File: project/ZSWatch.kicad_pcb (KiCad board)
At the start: 4 copper layers, 41 x 38 mm, 76 parts, among them IC1 nPM1300-QEXX, IC10 NTS0104GU12, IC11 FAN5622SX, IC2 APDS-9306-065, IC3 BMI270, IC4 BMP581, IC5 BME688, IC6 LIS2MDLTR, IC7 ESDALC6V1W5, IC8 AT25SL128A, IC9 DRV2603RUNT, M1 NORA-B106, X1 BATTERY, X10 GC9A01A_CST816S, X2 DOCK, X3 GPIO0, X4 GPIO1, X5 GPIO2, X6 GPIO3, X7 GND, X8 M+, X9 M-

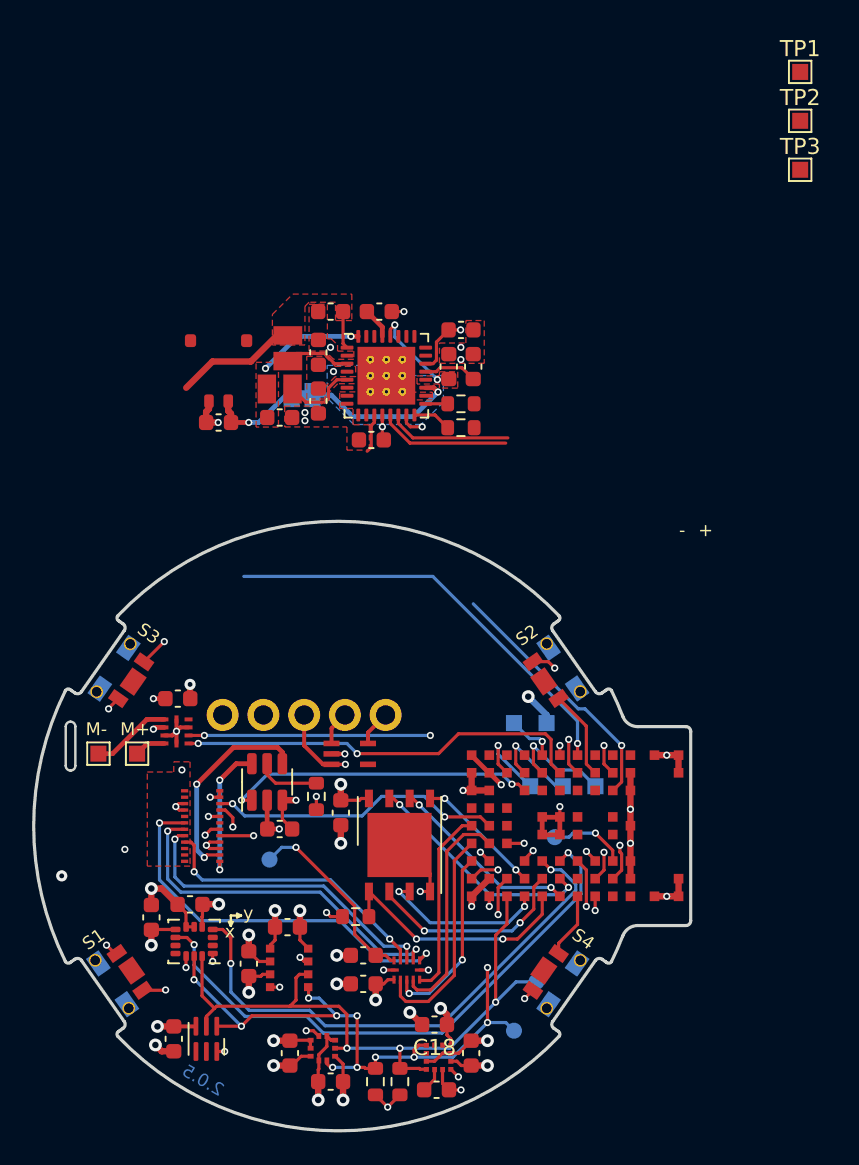
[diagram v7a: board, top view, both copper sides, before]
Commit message: - Add QR code library with link to the project - Change ISET resistor to 12k - Replace light sensor footprint with a version from our KiCad library - Rename the inner copper layers - Add KiBot file for production file generation - Import nPM1300 from test project - Remove pull down resistor from vibration driver IC enable - Split schematics into hierarical schematics - Add PCB variant for reduced sensor board - Add I2S microphone - Update all symbols and footprints
Signed-off-by: Daniel Kampert <DanielKampert@kampis-elektroecke.de>
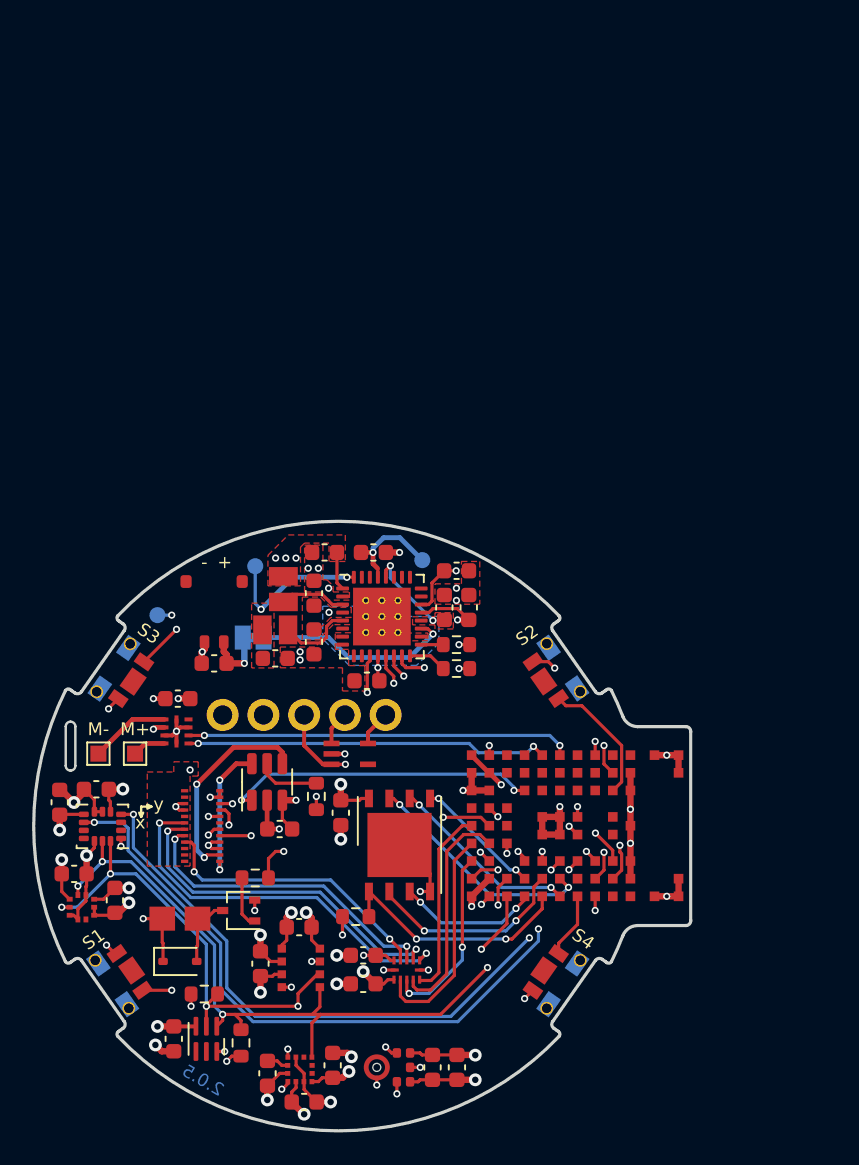
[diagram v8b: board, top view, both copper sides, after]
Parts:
- removed TP4: RESET, TestPoint:TestPoint_Pad_D1.0mm
- removed TP5: SCL, TestPoint:TestPoint_Pad_D1.0mm
- removed TP6: SDA, TestPoint:TestPoint_Pad_D1.0mm
- removed TP7: 3V3, TestPoint:TestPoint_Pad_D1.0mm
- removed the X3 at (171.3, 110.2)
- removed the X4 at (173.4, 110.2)
- removed the X5 at (175.4, 110.2)
- removed X6: GPIO3, TestPoint:TestPoint_Pad_1.0x1.0mm
- removed X7: GND, TestPoint:TestPoint_Pad_1.0x1.0mm
- added BZ1: Buzzer, CUI Devices:CMT-322-65-SMT-TR, F.Cu at (149.5, 118.5)
- added C22: 1u, Capacitor_SMD:C_0603_1608Metric, F.Cu at (165.2, 127.8)
- added C23: 200p, Capacitor_SMD:C_0603_1608Metric, F.Cu at (166.8, 127.8)
- added D1: BAS316, Diode_SMD:D_SOD-323, F.Cu at (149.5, 121.2)
- added MK1: SPH0645LM4H-B, Knowles:SPH0645LM4H-6_3.5x2.65mm, F.Cu at (162.5, 127.8)
- added Q1: BC817W, Package_TO_SOT_SMD:SOT-323_SC-70, F.Cu at (153.1, 118.0)
- added R6: 180R, Resistor_SMD:R_0603_1608Metric, F.Cu at (154.2, 116.0)
- TP1, TP2, TP3: footprint TestPoint:TestPoint_Pad_1.0x1.0mm -> TestPoint:TestPoint_Pad_D1.0mm; moved to B.Cu
- moved TP2 50.5 mm to (148.1, 99.6), turned to -90 degrees
- moved TP3 42.0 mm to (154.2, 96.5), turned to 180 degrees
- moved TP1 38.5 mm to (164.6, 96.1), turned to 180 degrees
- moved G*** 22.6 mm to (177.0, 112.6), turned to 90 degrees
- moved C15 20.6 mm to (142.9, 115.7), turned to 180 degrees
- moved IC4 17.4 mm to (143.4, 117.8), turned to 0 degrees
- moved J1 15.4 mm to (154.1, 101.0)
- moved C7 15.0 mm to (158.5, 95.7)
- moved C8 15.0 mm to (161.5, 95.7)
- moved C1 15.0 mm to (167.5, 99.1)
- moved C10 15.0 mm to (166.7, 96.8)
- moved C2 15.0 mm to (161.1, 103.7)
- moved C5 15.0 mm to (155.4, 102.3)
- moved C6 15.0 mm to (157.8, 101.2)
- moved C9 15.0 mm to (166.0, 99.1)
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- renumbered C23 to C24, C24 to C25, C22 to C26, C25 to C27, IC9 to IC10, IC10 to IC9, X10 to X3, X8 to X4, X9 to X5
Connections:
- C10 pad 1: VBUS -> /MCU/VBUS-MCU
- C19 pad 1: GND -> +1V8
- C19 pad 2: +1V8 -> GND
- C25 pad 1: DISPLAY_3V3 -> /MCU/VDD-Display
- C26 pad 1: +BATT -> /MCU/VBAT
- C27 pad 2: DISPLAY_3V3 -> /MCU/VDD-Display
- C3 pad 1: Net-(J1-A) -> /MCU/VBAT
- C8 pad 1: /Power Management/3V3-Display -> /MCU/VDD-Display
- IC1 pad 11: /Power Management/PMIC-INT -> /MCU/PMIC-INT
- IC1 pad 15: BTN_1 -> BTN_3
- IC1 pad 22: VBUS -> /MCU/VBUS-MCU
- IC1 pad 29: /Power Management/3V3-Display -> /MCU/VDD-Display
- IC10 pad 4: unconnected-(IC9-NC-Pad4) -> (no net)
- IC10 pad 7: +BATT -> /MCU/VBAT
- IC11 pad 3: DISPLAY_3V3 -> /MCU/VDD-Display
- IC3 pad 4: /MCU/LIS-INT1 -> /MCU/BMI270-INT1
- IC3 pad 9: /MCU/LIS-INT2 -> /MCU/BMI270-INT2
- IC4 pad 7: /MCU/BMP581_INT -> unconnected-(IC4-INT-Pad7)
- IC9 pad 11: DISPLAY_3V3 -> /MCU/VDD-Display
- J1 pad 1: Net-(J1-A) -> /MCU/VBAT
- M1 pad B6: unconnected-(M1B-P0.01/XL2-PadB6) -> BUZZER
- M1 pad B9: VBUS -> /MCU/VBUS-MCU
- M1 pad C8: GPIO0 -> unconnected-(M1B-P0.22-PadC8)
- M1 pad D8: GPIO1 -> unconnected-(M1B-P0.04/AIN0-PadD8)
- M1 pad E3: /MCU/LIS-INT1 -> MIC_SEL
- M1 pad E8: GPIO2 -> unconnected-(M1B-P0.05/AIN1-PadE8)
- M1 pad E9: GPIO3 -> DRV_VIB_EN
- M1 pad F3: /MCU/LIS-INT2 -> MIC_DATA
- M1 pad F8: DRV_VIB_EN -> unconnected-(M1C-P1.14-PadF8)
- M1 pad G3: /MCU/BMP581_INT -> MIC_BCLK
- M1 pad G4: unconnected-(M1C-P1.04-PadG4) -> /MCU/BMI270-INT2
- M1 pad G5: unconnected-(M1C-P1.08-PadG5) -> /MCU/BMI270-INT1
- M1 pad G8: BTN_3 -> unconnected-(M1C-P1.12-PadG8)
- M1 pad H8: BTN_2 -> unconnected-(M1B-P0.30-PadH8)
- M1 pad H9: unconnected-(M1C-P1.11-PadH9) -> /MCU/PMIC-INT
- M1 pad J7: unconnected-(M1C-P1.10-PadJ7) -> BTN_2
- M1 pad J8: unconnected-(M1B-P0.28/AIN7-PadJ8) -> BTN_3
- TP1 pad 1: /Power Management/3V3-Display -> /MCU/VDD-Display
- X1 pad 1: Net-(J1-A) -> /MCU/VBAT
- X3 pad 13: DISPLAY_3V3 -> /MCU/VDD-Display
- X3 pad 14: DISPLAY_3V3 -> /MCU/VDD-Display
- X3 pad 17: DISPLAY_3V3 -> /MCU/VDD-Display
- X3 pad 22: unconnected-(X10-NC-Pad22) -> (no net)
- X3 pad 23: DISPLAY_3V3 -> /MCU/VDD-Display
- X3 pad 24: DISPLAY_3V3 -> /MCU/VDD-Display
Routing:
- net /MCU/VDD-Display: track 0.00 -> 52.6 mm, vias 0 -> 4
- net /MCU/BMI270-INT2: track 0.00 -> 47.9 mm, vias 0 -> 3
- net /MCU/BMI270-INT1: track 0.00 -> 46.6 mm, vias 0 -> 3
- net /MCU/LIS-INT2: track 35.7 -> 0.00 mm, vias 2 -> 0
- net /MCU/LIS-INT1: track 33.3 -> 0.00 mm, vias 2 -> 0
- net +3V0: track 6.61 -> 37.4 mm, vias 2 -> 3
- net /MCU/SENSOR-SDA: track 50.6 -> 79.0 mm, vias 3 -> 7
- net unconnected-(M1C-P1.13-PadG9): track 26.7 -> 0.00 mm, vias 1 -> 0
- net DISPLAY_3V3: track 25.7 -> 0.00 mm, vias 3 -> 0
- net /MCU/SENSOR-SCL: track 56.5 -> 81.3 mm, vias 12 -> 6
- net /MCU/BMP581_INT: track 24.7 -> 0.00 mm, vias 2 -> 0
- net DISPLAY_EN: track 35.3 -> 14.1 mm, vias 3 -> 2
- net MIC_BCLK: track 0.00 -> 20.9 mm, vias 0 -> 2
- net +BATT: track 20.8 -> 0.00 mm, vias 3 -> 0
- net MIC_SEL: track 0.00 -> 20.1 mm, vias 0 -> 2
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- added copper zone on F.Cu, net /MCU/VDD-Display
- removed copper zone on F.Cu, net DISPLAY_3V3
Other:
- board text added: "Dielektrikum"
- board text added: "Inner1"
- board text added: "Inner2"
- board text removed: "Dielektrikum 1"
- board text removed: "Dielektrikum 2"
- board text removed: "Dielektrikum 3"
- board text removed: "Layer2"
- board text removed: "Layer3"
